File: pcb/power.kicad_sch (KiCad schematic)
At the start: 6 parts, among them U1 AMS1117-3.3

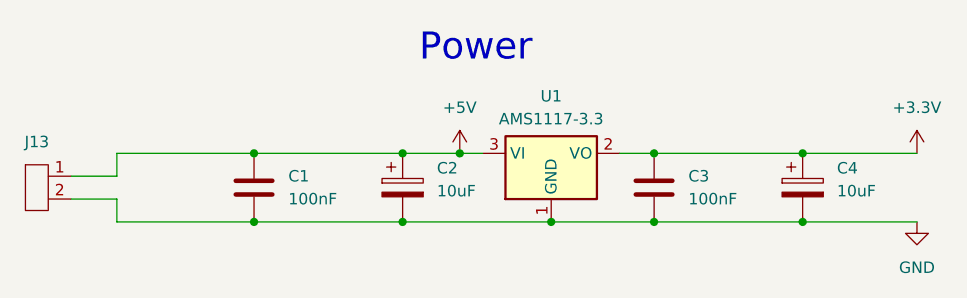
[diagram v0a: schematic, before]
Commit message: Finishing the carrier board with the new usb-c modul
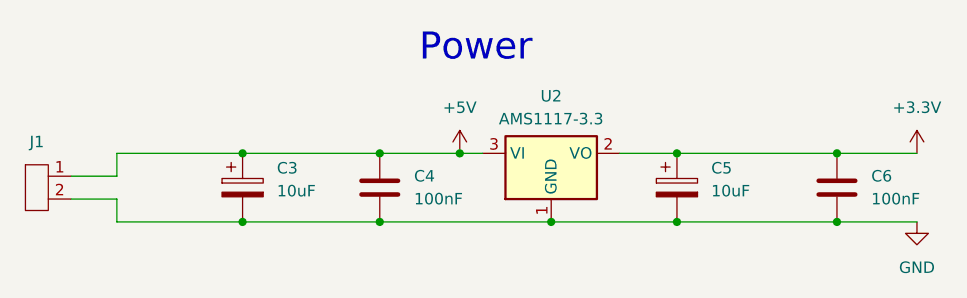
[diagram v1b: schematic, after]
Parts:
- removed C1, C3: 100nF, Resistor_SMD:R_0603_1608Metric_Pad0.98x0.95mm_HandSolder, symbol Device:C
- removed C2: 10uF, Capacitor_THT:CP_Radial_D5.0mm_P2.00mm, symbol Device:C_Polarized
- added C3: 10uF, Capacitor_THT:CP_Radial_D5.0mm_P2.00mm, symbol Device:C_Polarized
- added C4, C6: 100nF, Resistor_SMD:R_0603_1608Metric_Pad0.98x0.95mm_HandSolder, symbol Device:C
- renumbered C4 to C5, J13 to J1, U1 to U2
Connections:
- net +3.3V: now also C6.1
- net +5V: now also C3.1, C4.1
- net GND: now also C3.2, C4.2, C6.2
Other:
- moved on the sheet: C5
